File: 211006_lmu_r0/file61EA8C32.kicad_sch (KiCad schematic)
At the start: 15 parts, among them U8 ISO7761DBQ

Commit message: Updated lmu project with relative library paths and fixed broken symbols
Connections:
- net GND: now also C180.2, U8.8 (GND1)
- net +3V3: now reaches C180.1, U8.1 (Vcc1)
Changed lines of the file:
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@@
       (effects (font (size 1.27 1.27)) hide)
     )
+    (pin "1")
   )
   (symbol (lib_id "gnd_iso:GND_ISO") (at 127 110.49 0)
@@
       (effects (font (size 1.27 1.27)) hide)
     )
+    (pin "1")
   )
   (symbol (lib_id "Isolator:ISO7761DBQ") (at 144.78 93.98 0)

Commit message: Updated some components to make sourcing easier
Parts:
- C180, C181, R230, R231, R232, R233, R234, R235, R236, R237, R238, R239, R240, R241: Manufacturer (none) -> -; Part Number (none) -> -
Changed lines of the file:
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@@
+      (effects (font (size 1.27 1.27)) hide)
+    )
+    (property "Part Number" "-" (id 4) (at 194.31 86.36 0)
+      (effects (font (size 1.27 1.27)) hide)
+    )
+    (property "Manufacturer" "-" (id 5) (at 194.31 86.36 0)
       (effects (font (size 1.27 1.27)) hide)
     )
@@
       (effects (font (size 1.27 1.27)) hide)
     )
+    (property "Part Number" "-" (id 4) (at 194.31 88.9 0)
+      (effects (font (size 1.27 1.27)) hide)
+    )
+    (property "Manufacturer" "-" (id 5) (at 194.31 88.9 0)
+      (effects (font (size 1.27 1.27)) hide)
+    )
     (pin "1")
     (pin "2")
@@
       (effects (font (size 1.27 1.27)) hide)
     )
+    (property "Part Number" "-" (id 4) (at 194.31 91.44 0)
+      (effects (font (size 1.27 1.27)) hide)
+    )
+    (property "Manufacturer" "-" (id 5) (at 194.31 91.44 0)
+      (effects (font (size 1.27 1.27)) hide)
+    )
     (pin "1")
     (pin "2")
@@
       (effects (font (size 1.27 1.27)) hide)
     )
+    (property "Part Number" "-" (id 4) (at 194.31 93.98 0)
+      (effects (font (size 1.27 1.27)) hide)
+    )
+    (property "Manufacturer" "-" (id 5) (at 194.31 93.98 0)
+      (effects (font (size 1.27 1.27)) hide)
+    )
     (pin "1")
     (pin "2")
@@
       (effects (font (size 1.27 1.27)) hide)
     )
+    (property "Part Number" "-" (id 4) (at 194.31 96.52 0)
+      (effects (font (size 1.27 1.27)) hide)
+    )
+    (property "Manufacturer" "-" (id 5) (at 194.31 96.52 0)
+      (effects (font (size 1.27 1.27)) hide)
+    )
     (pin "1")
     (pin "2")
@@
       (effects (font (size 1.27 1.27)) hide)
     )
+    (property "Part Number" "-" (id 4) (at 194.31 99.06 0)
+      (effects (font (size 1.27 1.27)) hide)
+    )
+    (property "Manufacturer" "-" (id 5) (at 194.31 99.06 0)
+      (effects (font (size 1.27 1.27)) hide)
+    )
     (pin "1")
     (pin "2")
@@
     )
     (property "Datasheet" "~" (id 3) (at 160.02 81.28 0)
+      (effects (font (size 1.27 1.27)) hide)
+    )
+    (property "Part Number" "-" (id 4) (at 160.02 81.28 0)
+      (effects (font (size 1.27 1.27)) hide)
+    )
+    (property "Manufacturer" "-" (id 5) (at 160.02 81.28 0)
       (effects (font (size 1.27 1.27)) hide)
     )
@@
       (effects (font (size 1.27 1.27)) hide)
     )
+    (property "Part Number" "-" (id 4) (at 95.25 86.36 0)
+      (effects (font (size 1.27 1.27)) hide)
+    )
+    (property "Manufacturer" "-" (id 5) (at 95.25 86.36 0)
+      (effects (font (size 1.27 1.27)) hide)
+    )
     (pin "1")
     (pin "2")
@@
       (effects (font (size 1.27 1.27)) hide)
     )
+    (property "Part Number" "-" (id 4) (at 95.25 88.9 0)
+      (effects (font (size 1.27 1.27)) hide)
+    )
+    (property "Manufacturer" "-" (id 5) (at 95.25 88.9 0)
+      (effects (font (size 1.27 1.27)) hide)
+    )
     (pin "1")
     (pin "2")
@@
       (effects (font (size 1.27 1.27)) hide)
     )
+    (property "Part Number" "-" (id 4) (at 95.25 91.44 0)
+      (effects (font (size 1.27 1.27)) hide)
+    )
+    (property "Manufacturer" "-" (id 5) (at 95.25 91.44 0)
+      (effects (font (size 1.27 1.27)) hide)
+    )
     (pin "1")
     (pin "2")
@@
       (effects (font (size 1.27 1.27)) hide)
     )
+    (property "Part Number" "-" (id 4) (at 95.25 93.98 0)
+      (effects (font (size 1.27 1.27)) hide)
+    )
+    (property "Manufacturer" "-" (id 5) (at 95.25 93.98 0)
+      (effects (font (size 1.27 1.27)) hide)
+    )
     (pin "1")
     (pin "2")
@@
       (effects (font (size 1.27 1.27)) hide)
     )
+    (property "Part Number" "-" (id 4) (at 95.25 96.52 0)
+      (effects (font (size 1.27 1.27)) hide)
+    )
+    (property "Manufacturer" "-" (id 5) (at 95.25 96.52 0)
+      (effects (font (size 1.27 1.27)) hide)
+    )
     (pin "1")
     (pin "2")
@@
     )
     (property "Datasheet" "~" (id 3) (at 95.25 99.06 0)
+      (effects (font (size 1.27 1.27)) hide)
+    )
+    (property "Part Number" "-" (id 4) (at 95.25 99.06 0)
+      (effects (font (size 1.27 1.27)) hide)
+    )
+    (property "Manufacturer" "-" (id 5) (at 95.25 99.06 0)
       (effects (font (size 1.27 1.27)) hide)
     )
@@
       (effects (font (size 1.27 1.27)) hide)
     )
+    (property "Part Number" "-" (id 4) (at 127 81.28 0)
+      (effects (font (size 1.27 1.27)) hide)
+    )
+    (property "Manufacturer" "-" (id 5) (at 127 81.28 0)
+      (effects (font (size 1.27 1.27)) hide)
+    )

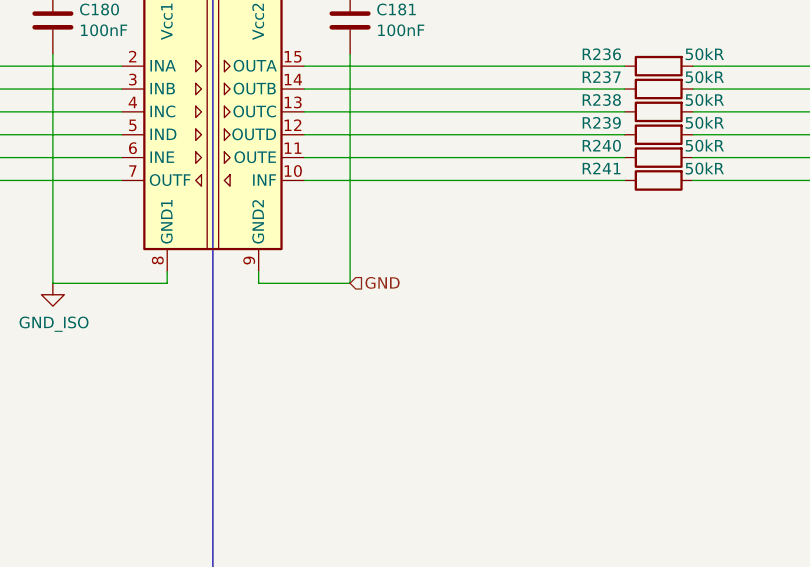
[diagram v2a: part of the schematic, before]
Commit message: fixed footprints for headers, started planning out zones
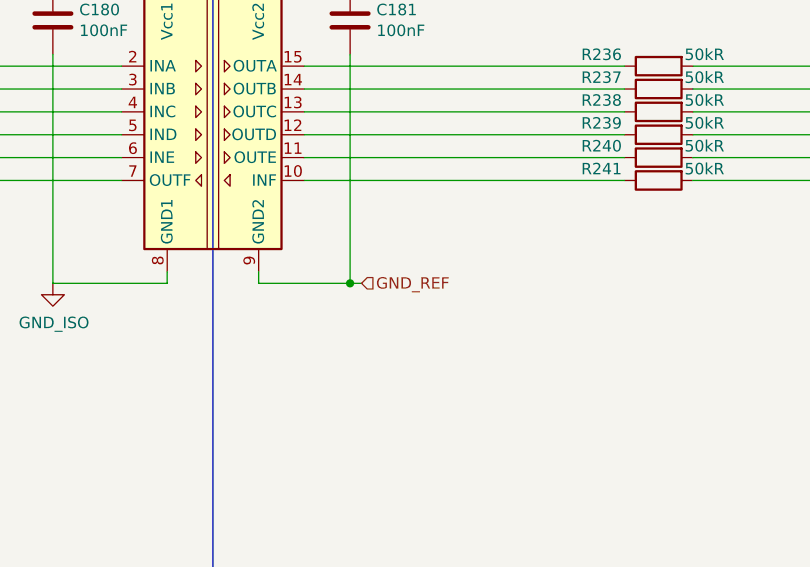
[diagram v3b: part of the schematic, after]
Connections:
- net +3V3 renamed +3V3_ISO
- net GND renamed GND_ISO
- net GND_ISO: no longer C181.2, U8.9 (GND2)
- new net GND_REF: C181.2, U8.9 (GND2)
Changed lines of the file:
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@@
 (kicad_sch (version 20211123) (generator eeschema)
   (paper "A4")
+  (junction (at 160.02 110.49) (diameter 0) (color 0 0 0 0)
+  )
   (wire (pts (xy 127 110.49) (xy 139.7 110.49))
     (stroke (width 0) (type default) (color 0 0 0 0))
@@
   )
   (wire (pts (xy 91.44 88.9) (xy 68.58 88.9))
+    (stroke (width 0) (type default) (color 0 0 0 0))
+  )
+  (wire (pts (xy 160.02 110.49) (xy 161.29 110.49))
     (stroke (width 0) (type default) (color 0 0 0 0))
   )
@@
     (effects (font (size 1.27 1.27)) (justify left))
   )
+  (hierarchical_label "GND_REF" (shape input) (at 161.29 110.49 0)
+    (effects (font (size 1.27 1.27)) (justify left))
+  )
   (hierarchical_label "SDO_ISO" (shape input) (at 68.58 99.06 180)
     (effects (font (size 1.27 1.27)) (justify right))
@@
   )
   (hierarchical_label "VREG" (shape input) (at 160.02 74.93 0)
-    (effects (font (size 1.27 1.27)) (justify left))
-  )
-  (hierarchical_label "GND" (shape input) (at 160.02 110.49 0)
     (effects (font (size 1.27 1.27)) (justify left))
   )
@@
   (symbol (lib_id "+3v3_iso:+3V3_ISO") (at 127 74.93 0)
     (in_bom yes) (on_board yes)
-    (property "Reference" "#PWR075" (id 0) (at 127 78.74 0)
+    (property "Reference" "#PWR0104" (id 0) (at 127 78.74 0)
       (effects (font (size 1.27 1.27)) hide)
     )
@@
   (symbol (lib_id "gnd_iso:GND_ISO") (at 127 110.49 0)
     (in_bom yes) (on_board yes)
-    (property "Reference" "#PWR076" (id 0) (at 127 116.84 0)
-      (effects (font (size 1.27 1.27)) hide)
-    )
+    (property "Reference" "#PWR0105" (id 0) (at 127 116.84 0)
+      (effects (font (size 1.27 1.27)) hide)
+    )

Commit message: merge PCB
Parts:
- removed U8: ISO7761DBQ, Package_SO:SSOP-16_3.9x4.9mm_P0.635mm, symbol Isolator:ISO7761DBQ
- added U8: ADuM7641A, Package_SO:QSOP-20_3.9x8.7mm_P0.635mm, symbol Isolator:ADuM7641A
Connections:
- net +3V3_ISO: now also U8.1 (VDD1A), U8.7 (VDD1B)
- net GND_ISO: now also U8.10 (GND1), U8.2 (GND1)
- net GND_REF: now also U8.11 (GND2), U8.19 (GND2)
- net SDI: now also R241.2; no longer R240.2
- net SDI_ISO: now also R235.2; no longer R234.2
- net SDO: now also R240.2; no longer R241.2
- net SDO_ISO: now also R234.2; no longer R235.2
- net VREG: now also U8.14 (VDD2B), U8.20 (VDD2A)
- net at R236.1: now also U8.18 (VOA)
- net at R237.1: now also U8.17 (VOB)
- net at R238.1: now also U8.16 (VOC)
- net at R239.1: now also U8.15 (VOD)
- net at R240.1: now also U8.13 (VIE)
- net at R241.1: now also U8.12 (VOF)
- net at R230.1: now also U8.3 (VIA)
- net at R231.1: now also U8.4 (VIB)
- net at R232.1: now also U8.5 (VIC)
- net at R233.1: now also U8.6 (VID)
- net at R234.1: now also U8.8 (VOE)
- net at R235.1: now also U8.9 (VIF)
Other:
- moved on the sheet: C180

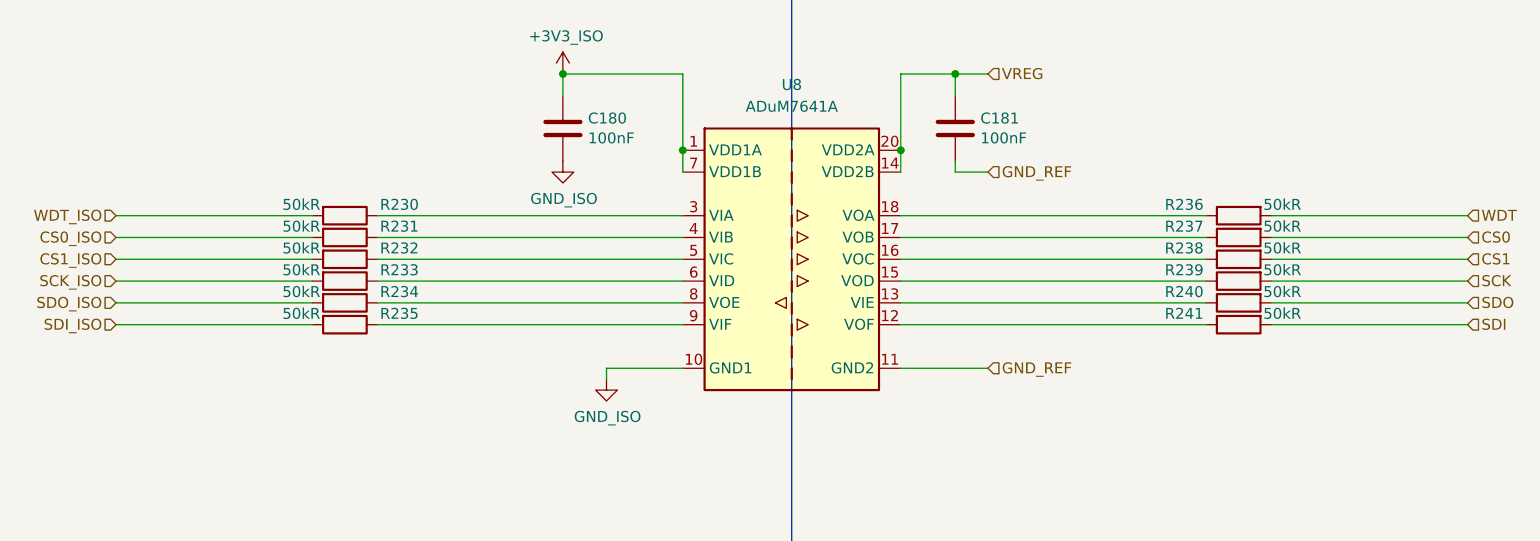
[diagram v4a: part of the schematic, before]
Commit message: Routed vehicle section
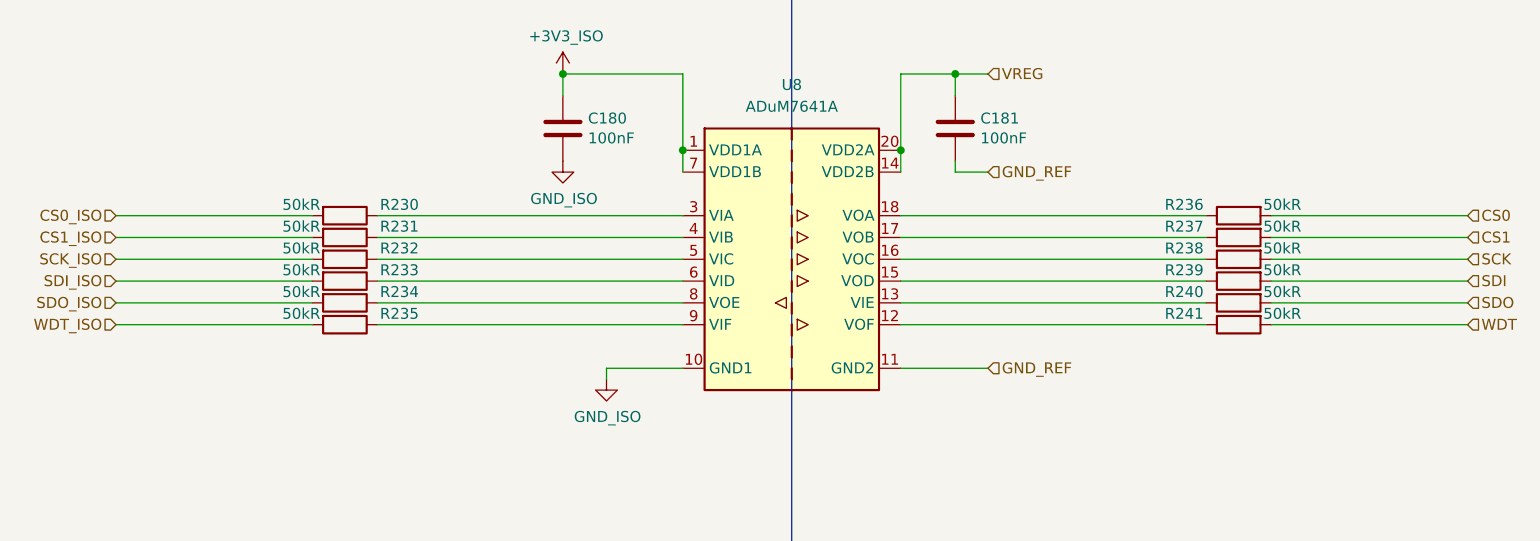
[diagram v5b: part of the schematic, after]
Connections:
- net CS0: now also R236.2; no longer R237.2
- net CS0_ISO: now also R230.2; no longer R231.2
- net CS1: now also R237.2; no longer R238.2
- net CS1_ISO: now also R231.2; no longer R232.2
- net SCK: now also R238.2; no longer R239.2
- net SCK_ISO: now also R232.2; no longer R233.2
- net SDI: now also R239.2; no longer R241.2
- net SDI_ISO: now also R233.2; no longer R235.2
- net WDT: now also R241.2; no longer R236.2
- net WDT_ISO: now also R235.2; no longer R230.2
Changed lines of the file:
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@@
     (stroke (width 0) (type default) (color 0 0 0 0))
   )
-  (hierarchical_label "WDT_ISO" (shape input) (at 66.04 93.98 180)
+  (hierarchical_label "SDI_ISO" (shape input) (at 66.04 101.6 180)
     (effects (font (size 1.27 1.27)) (justify right))
-  )
-  (hierarchical_label "SDI" (shape input) (at 223.52 106.68 0)
-    (effects (font (size 1.27 1.27)) (justify left))
-  )
-  (hierarchical_label "SCK" (shape input) (at 223.52 101.6 0)
-    (effects (font (size 1.27 1.27)) (justify left))
   )
   (hierarchical_label "SDO_ISO" (shape input) (at 66.04 104.14 180)
     (effects (font (size 1.27 1.27)) (justify right))
   )
-  (hierarchical_label "CS0" (shape input) (at 223.52 96.52 0)
+  (hierarchical_label "SCK" (shape input) (at 223.52 99.06 0)
     (effects (font (size 1.27 1.27)) (justify left))
   )
-  (hierarchical_label "WDT" (shape input) (at 223.52 93.98 0)
+  (hierarchical_label "CS0_ISO" (shape input) (at 66.04 93.98 180)
+    (effects (font (size 1.27 1.27)) (justify right))
+  )
+  (hierarchical_label "SDI" (shape input) (at 223.52 101.6 0)
     (effects (font (size 1.27 1.27)) (justify left))
-  )
-  (hierarchical_label "CS1" (shape input) (at 223.52 99.06 0)
-    (effects (font (size 1.27 1.27)) (justify left))
-  )
-  (hierarchical_label "SDI_ISO" (shape input) (at 66.04 106.68 180)
-    (effects (font (size 1.27 1.27)) (justify right))
   )
   (hierarchical_label "GND_REF" (shape input) (at 167.64 88.9 0)
@@
     (effects (font (size 1.27 1.27)) (justify left))
   )
-  (hierarchical_label "CS0_ISO" (shape input) (at 66.04 96.52 180)
+  (hierarchical_label "SCK_ISO" (shape input) (at 66.04 99.06 180)
+    (effects (font (size 1.27 1.27)) (justify right))
+  )
+  (hierarchical_label "WDT" (shape input) (at 223.52 106.68 0)
+    (effects (font (size 1.27 1.27)) (justify left))
+  )
+  (hierarchical_label "WDT_ISO" (shape input) (at 66.04 106.68 180)
+    (effects (font (size 1.27 1.27)) (justify right))
+  )
+  (hierarchical_label "CS1_ISO" (shape input) (at 66.04 96.52 180)
     (effects (font (size 1.27 1.27)) (justify right))
   )
@@
     (effects (font (size 1.27 1.27)) (justify left))
   )
-  (hierarchical_label "SCK_ISO" (shape input) (at 66.04 101.6 180)
-    (effects (font (size 1.27 1.27)) (justify right))
+  (hierarchical_label "CS1" (shape input) (at 223.52 96.52 0)
+    (effects (font (size 1.27 1.27)) (justify left))
   )
   (hierarchical_label "VREG" (shape input) (at 167.64 77.47 0)
     (effects (font (size 1.27 1.27)) (justify left))
   )
-  (hierarchical_label "CS1_ISO" (shape input) (at 66.04 99.06 180)
-    (effects (font (size 1.27 1.27)) (justify right))
+  (hierarchical_label "CS0" (shape input) (at 223.52 93.98 0)
+    (effects (font (size 1.27 1.27)) (justify left))
   )
   (symbol (lib_id "+3v3_iso:+3V3_ISO") (at 118.11 77.47 0)
